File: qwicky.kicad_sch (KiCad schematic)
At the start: 53 parts, among them J1 Conn_02x05_Odd_Even, J2 Conn_01x02, J4 Conn_01x04, J5 Conn_01x02, J6 Conn_01x02, U1 STM32F407VETx, U2 AMS1117-3.3

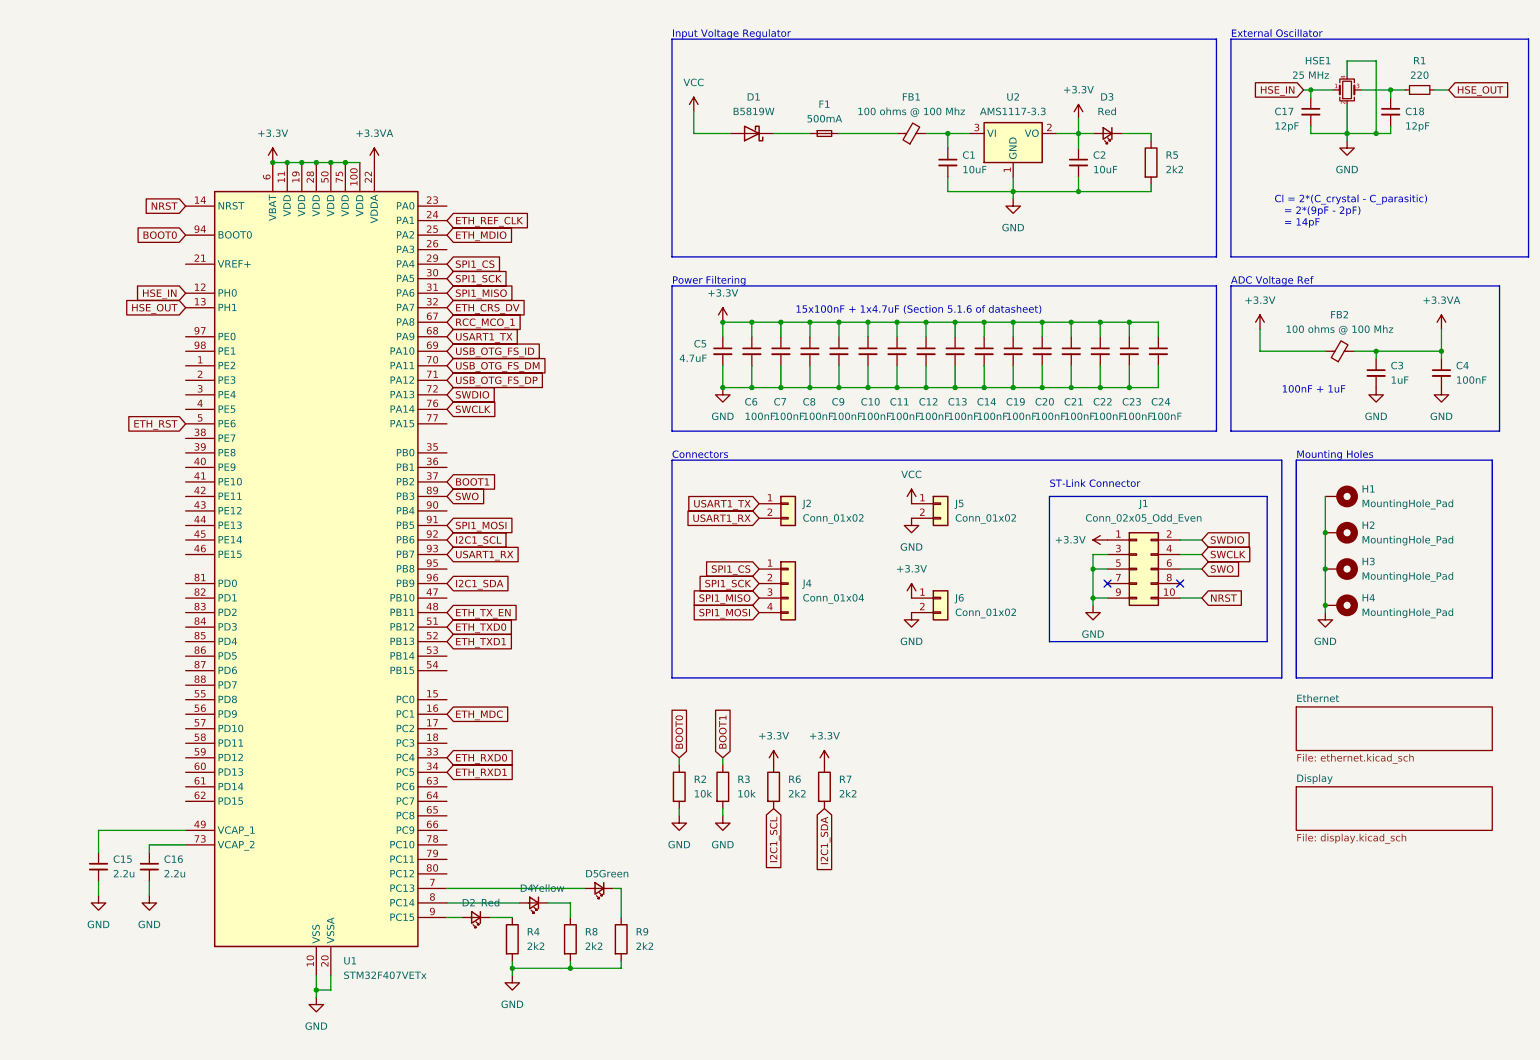
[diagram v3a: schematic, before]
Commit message: Added keyboard matrix schematic
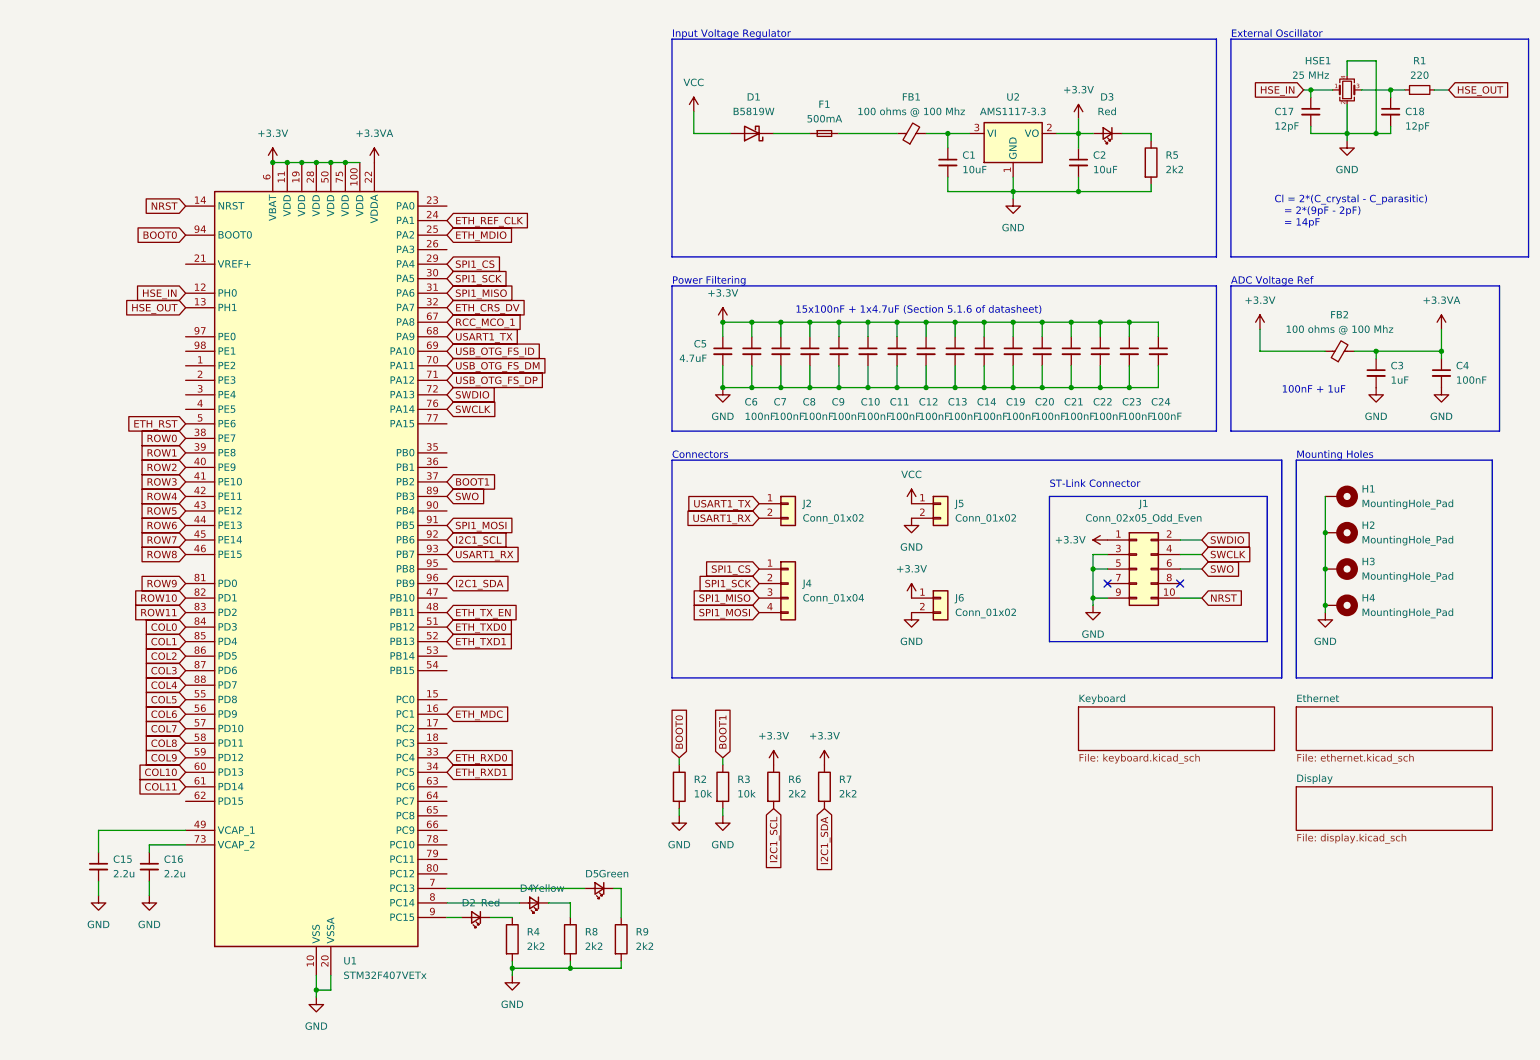
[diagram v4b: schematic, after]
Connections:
- net ROW0: now reaches U1.38 (PE7)
- net ROW1: now reaches U1.39 (PE8)
- net ROW2: now reaches U1.40 (PE9)
- net ROW3: now reaches U1.41 (PE10)
- net ROW4: now reaches U1.42 (PE11)
- net ROW5: now reaches U1.43 (PE12)
- net ROW6: now reaches U1.44 (PE13)
- net ROW7: now reaches U1.45 (PE14)
- net ROW8: now reaches U1.46 (PE15)
- net COL5: now reaches U1.55 (PD8)
- net COL6: now reaches U1.56 (PD9)
- net COL7: now reaches U1.57 (PD10)
- net COL8: now reaches U1.58 (PD11)
- net COL9: now reaches U1.59 (PD12)
- net COL10: now reaches U1.60 (PD13)
- net COL11: now reaches U1.61 (PD14)
- net ROW9: now reaches U1.81 (PD0)
- net ROW10: now reaches U1.82 (PD1)
- net ROW11: now reaches U1.83 (PD2)
- net COL0: now reaches U1.84 (PD3)
- net COL1: now reaches U1.85 (PD4)
- net COL2: now reaches U1.86 (PD5)
- net COL3: now reaches U1.87 (PD6)
- net COL4: now reaches U1.88 (PD7)
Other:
- added sheet Keyboard (keyboard.kicad_sch)
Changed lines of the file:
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@@
+    )
+  )
+  (global_label "ROW3" (shape input) (at 44.45 95.25 180) (fields_autoplaced)
+    (effects (font (size 1.27 1.27)) (justify right))
+    (property "Intersheetrefs" "${INTERSHEET_REFS}" (at 36.2034 95.25 0)
+      (effects (font (size 1.27 1.27)) (justify right) hide)
     )
   )
@@
     )
   )
+  (global_label "ROW7" (shape input) (at 44.45 105.41 180) (fields_autoplaced)
+    (effects (font (size 1.27 1.27)) (justify right))
+    (property "Intersheetrefs" "${INTERSHEET_REFS}" (at 36.2034 105.41 0)
+      (effects (font (size 1.27 1.27)) (justify right) hide)
+    )
+  )
+  (global_label "COL7" (shape input) (at 44.45 138.43 180) (fields_autoplaced)
+    (effects (font (size 1.27 1.27)) (justify right))
+    (property "Intersheetrefs" "${INTERSHEET_REFS}" (at 36.6267 138.43 0)
+      (effects (font (size 1.27 1.27)) (justify right) hide)
+    )
+  )
+  (global_label "COL11" (shape input) (at 44.45 148.59 180) (fields_autoplaced)
+    (effects (font (size 1.27 1.27)) (justify right))
+    (property "Intersheetrefs" "${INTERSHEET_REFS}" (at 35.4172 148.59 0)
+      (effects (font (size 1.27 1.27)) (justify right) hide)
+    )
+  )
   (global_label "SPI1_MISO" (shape input) (at 144.78 115.57 180) (fields_autoplaced)
     (effects (font (size 1.27 1.27)) (justify right))
@@
     )
   )
+  (global_label "COL1" (shape input) (at 44.45 123.19 180) (fields_autoplaced)
+    (effects (font (size 1.27 1.27)) (justify right))
+    (property "Intersheetrefs" "${INTERSHEET_REFS}" (at 36.6267 123.19 0)
+      (effects (font (size 1.27 1.27)) (justify right) hide)
+    )
+  )
+  (global_label "ROW2" (shape input) (at 44.45 92.71 180) (fields_autoplaced)
+    (effects (font (size 1.27 1.27)) (justify right))
+    (property "Intersheetrefs" "${INTERSHEET_REFS}" (at 36.2034 92.71 0)
+      (effects (font (size 1.27 1.27)) (justify right) hide)
+    )
+  )
+  (global_label "ROW6" (shape input) (at 44.45 102.87 180) (fields_autoplaced)
+    (effects (font (size 1.27 1.27)) (justify right))
+    (property "Intersheetrefs" "${INTERSHEET_REFS}" (at 36.2034 102.87 0)
+      (effects (font (size 1.27 1.27)) (justify right) hide)
+    )
+  )
+  (global_label "ROW10" (shape input) (at 44.45 115.57 180) (fields_autoplaced)
+    (effects (font (size 1.27 1.27)) (justify right))
+    (property "Intersheetrefs" "${INTERSHEET_REFS}" (at 34.9939 115.57 0)
+      (effects (font (size 1.27 1.27)) (justify right) hide)
+    )
+  )
   (global_label "SPI1_MOSI" (shape input) (at 90.17 102.87 0) (fields_autoplaced)
     (effects (font (size 1.27 1.27)) (justify left))
@@
     )
   )
+  (global_label "ROW5" (shape input) (at 44.45 100.33 180) (fields_autoplaced)
+    (effects (font (size 1.27 1.27)) (justify right))
+    (property "Intersheetrefs" "${INTERSHEET_REFS}" (at 36.2034 100.33 0)
+      (effects (font (size 1.27 1.27)) (justify right) hide)
+    )
+  )
+  (global_label "COL8" (shape input) (at 44.45 140.97 180) (fields_autoplaced)
+    (effects (font (size 1.27 1.27)) (justify right))
+    (property "Intersheetrefs" "${INTERSHEET_REFS}" (at 36.6267 140.97 0)
+      (effects (font (size 1.27 1.27)) (justify right) hide)
+    )
+  )
   (global_label "USART1_RX" (shape input) (at 144.78 101.6 180) (fields_autoplaced)
     (effects (font (size 1.27 1.27)) (justify right))
@@
     )
   )
+  (global_label "ROW11" (shape input) (at 44.45 118.11 180) (fields_autoplaced)
+    (effects (font (size 1.27 1.27)) (justify right))
+    (property "Intersheetrefs" "${INTERSHEET_REFS}" (at 34.9939 118.11 0)
+      (effects (font (size 1.27 1.27)) (justify right) hide)
+    )
+  )
+  (global_label "ROW4" (shape input) (at 44.45 97.79 180) (fields_autoplaced)
+    (effects (font (size 1.27 1.27)) (justify right))
+    (property "Intersheetrefs" "${INTERSHEET_REFS}" (at 36.2034 97.79 0)
+      (effects (font (size 1.27 1.27)) (justify right) hide)
+    )
+  )
+  (global_label "COL6" (shape input) (at 44.45 135.89 180) (fields_autoplaced)
+    (effects (font (size 1.27 1.27)) (justify right))
+    (property "Intersheetrefs" "${INTERSHEET_REFS}" (at 36.6267 135.89 0)
+      (effects (font (size 1.27 1.27)) (justify right) hide)
+    )
+  )
   (global_label "SPI1_CS" (shape input) (at 90.17 57.15 0) (fields_autoplaced)
     (effects (font (size 1.27 1.27)) (justify left))
@@
     )
   )
+  (global_label "COL4" (shape input) (at 44.45 130.81 180) (fields_autoplaced)
+    (effects (font (size 1.27 1.27)) (justify right))
+    (property "Intersheetrefs" "${INTERSHEET_REFS}" (at 36.6267 130.81 0)
+      (effects (font (size 1.27 1.27)) (justify right) hide)
+    )
+  )
+  (global_label "COL0" (shape input) (at 44.45 120.65 180) (fields_autoplaced)
+    (effects (font (size 1.27 1.27)) (justify right))
+    (property "Intersheetrefs" "${INTERSHEET_REFS}" (at 36.6267 120.65 0)
+      (effects (font (size 1.27 1.27)) (justify right) hide)
+    )
+  )
   (global_label "ETH_RST" (shape input) (at 44.45 85.09 180) (fields_autoplaced)
     (effects (font (size 1.27 1.27)) (justify right))
@@
     )
   )
+  (global_label "COL9" (shape input) (at 44.45 143.51 180) (fields_autoplaced)
+    (effects (font (size 1.27 1.27)) (justify right))
+    (property "Intersheetrefs" "${INTERSHEET_REFS}" (at 36.6267 143.51 0)
+      (effects (font (size 1.27 1.27)) (justify right) hide)
+    )
+  )
   (global_label "ETH_TX_EN" (shape input) (at 90.17 118.11 0) (fields_autoplaced)
     (effects (font (size 1.27 1.27)) (justify left))
@@
     )
   )
+  (global_label "COL5" (shape input) (at 44.45 133.35 180) (fields_autoplaced)
+    (effects (font (size 1.27 1.27)) (justify right))
+    (property "Intersheetrefs" "${INTERSHEET_REFS}" (at 36.6267 133.35 0)
+      (effects (font (size 1.27 1.27)) (justify right) hide)
+    )
+  )
   (global_label "HSE_IN" (shape input) (at 44.45 62.23 180) (fields_autoplaced)
     (effects (font (size 1.27 1.27)) (justify right))
@@
     )
   )
+  (global_label "ROW8" (shape input) (at 44.45 107.95 180) (fields_autoplaced)
+    (effects (font (size 1.27 1.27)) (justify right))
+    (property "Intersheetrefs" "${INTERSHEET_REFS}" (at 36.2034 107.95 0)
+      (effects (font (size 1.27 1.27)) (justify right) hide)
+    )
+  )
+  (global_label "ROW9" (shape input) (at 44.45 113.03 180) (fields_autoplaced)
+    (effects (font (size 1.27 1.27)) (justify right))
+    (property "Intersheetrefs" "${INTERSHEET_REFS}" (at 36.2034 113.03 0)
+      (effects (font (size 1.27 1.27)) (justify right) hide)
+    )
+  )
   (global_label "SWO" (shape input) (at 90.17 97.79 0) (fields_autoplaced)
     (effects (font (size 1.27 1.27)) (justify left))
@@
     )
   )
+  (global_label "COL2" (shape input) (at 44.45 125.73 180) (fields_autoplaced)
+    (effects (font (size 1.27 1.27)) (justify right))
+    (property "Intersheetrefs" "${INTERSHEET_REFS}" (at 36.6267 125.73 0)
+      (effects (font (size 1.27 1.27)) (justify right) hide)
+    )
+  )
   (global_label "I2C1_SDA" (shape input) (at 90.17 113.03 0) (fields_autoplaced)
     (effects (font (size 1.27 1.27)) (justify left))
@@
     )
   )
+  (global_label "ROW1" (shape input) (at 44.45 90.17 180) (fields_autoplaced)
+    (effects (font (size 1.27 1.27)) (justify right))
+    (property "Intersheetrefs" "${INTERSHEET_REFS}" (at 36.2034 90.17 0)
+      (effects (font (size 1.27 1.27)) (justify right) hide)
+    )
+  )
   (global_label "ETH_TXD1" (shape input) (at 90.17 123.19 0) (fields_autoplaced)
     (effects (font (size 1.27 1.27)) (justify left))
@@
     )
   )
+  (global_label "COL3" (shape input) (at 44.45 128.27 180) (fields_autoplaced)
+    (effects (font (size 1.27 1.27)) (justify right))
+    (property "Intersheetrefs" "${INTERSHEET_REFS}" (at 36.6267 128.27 0)
+      (effects (font (size 1.27 1.27)) (justify right) hide)
+    )
+  )
+  (global_label "COL10" (shape input) (at 44.45 146.05 180) (fields_autoplaced)
+    (effects (font (size 1.27 1.27)) (justify right))
+    (property "Intersheetrefs" "${INTERSHEET_REFS}" (at 35.4172 146.05 0)
+      (effects (font (size 1.27 1.27)) (justify right) hide)
+    )
+  )
   (global_label "SPI1_MOSI" (shape input) (at 144.78 118.11 180) (fields_autoplaced)
     (effects (font (size 1.27 1.27)) (justify right))
@@
     (effects (font (size 1.27 1.27)) (justify right))
     (property "Intersheetrefs" "${INTERSHEET_REFS}" (at 33.1796 64.77 0)
+      (effects (font (size 1.27 1.27)) (justify right) hide)
+    )
+  )
+  (global_label "ROW0" (shape input) (at 44.45 87.63 180) (fields_autoplaced)
+    (effects (font (size 1.27 1.27)) (justify right))
+    (property "Intersheetrefs" "${INTERSHEET_REFS}" (at 36.2034 87.63 0)
       (effects (font (size 1.27 1.27)) (justify right) hide)
     )
@@
       )
     )
+  )
+  (sheet (at 200.66 134.62) (size 34.29 7.62) (fields_autoplaced)
+    (stroke (width 0.1524) (type solid))
+    (fill (color 0 0 0 0.0000))
+    (property "Sheetname" "Keyboard" (at 200.66 133.9084 0)
+      (effects (font (size 1.27 1.27)) (justify left bottom))
+    )
+    (property "Sheetfile" "keyboard.kicad_sch" (at 200.66 142.8246 0)
+      (effects (font (size 1.27 1.27)) (justify left top))
+    )
+    (instances
+      (project "qwicky"
+        (path "/bd74968a-27d8-4281-bec5-c611f9e7fcfb" (page "4"))
+      )
+    )
